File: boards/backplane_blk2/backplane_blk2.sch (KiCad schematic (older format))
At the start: 1 part, among them J1 Conn_04x24

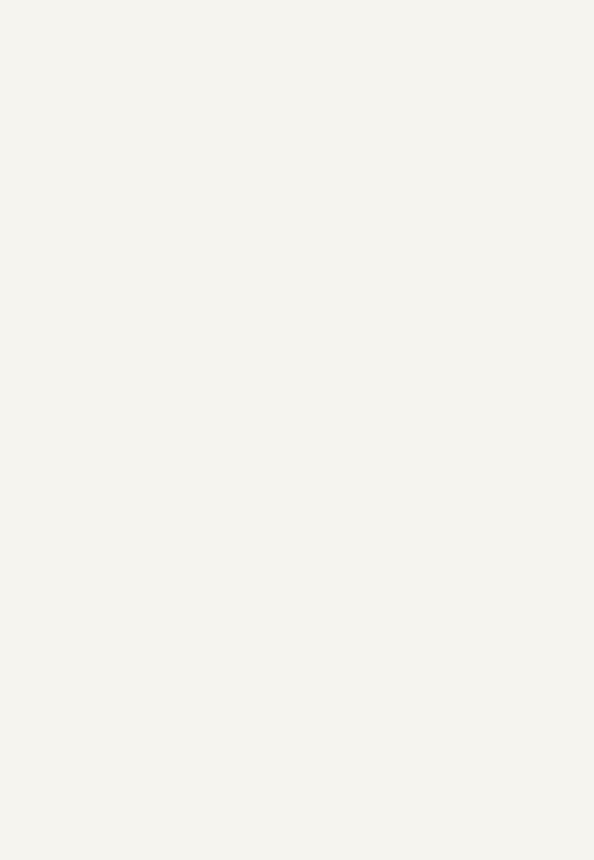
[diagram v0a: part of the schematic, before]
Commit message: Backplane board: new name, and initial integration of DIN-41612 3x32 C connector
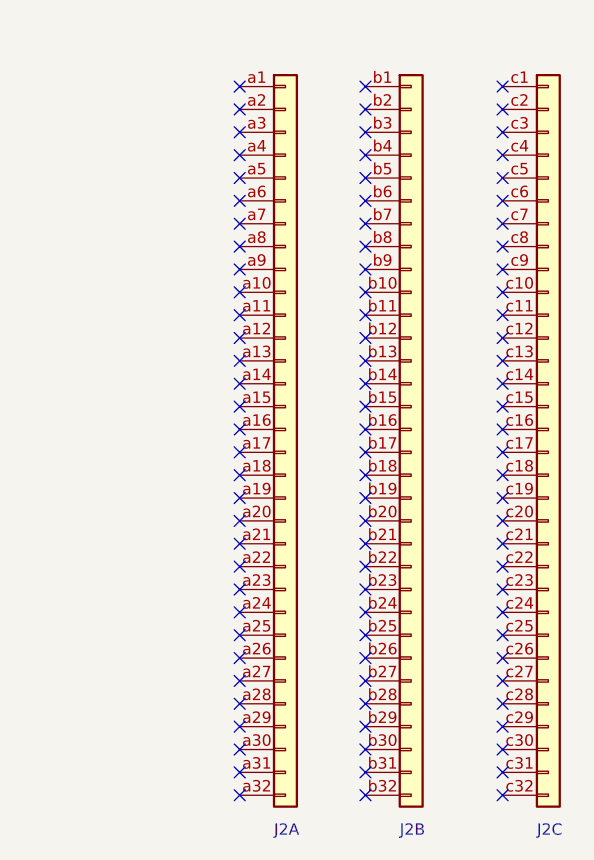
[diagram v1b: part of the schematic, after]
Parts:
- added J2: DIN41612_03x32_C, Connector_DIN:DIN41612_C_3x32_Female_Vertical_THT, symbol lachesis:DIN41612_03x32_C
- J1: footprint (none) -> lachesis:Rope_Connector
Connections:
- no-connect marks 6 -> 102
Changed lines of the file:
@@
 F 0 "J1" H 2400 700 50  0000 L CNN
 F 1 "Conn_04x24" H 2580 1951 50  0001 L CNN
-F 2 "" H 2500 2050 50  0001 C CNN
+F 2 "lachesis:Rope_Connector" H 2500 2050 50  0001 C CNN
 F 3 "~" H 2500 2050 50  0001 C CNN
 	1    2500 2050
@@
 F 0 "J1" H 3200 700 50  0000 L CNN
 F 1 "Conn_04x24" H 3380 1951 50  0001 L CNN
-F 2 "" H 3300 2050 50  0001 C CNN
+F 2 "lachesis:Rope_Connector" H 3300 2050 50  0001 C CNN
 F 3 "~" H 3300 2050 50  0001 C CNN
 	2    3300 2050
@@
 F 0 "J1" H 4000 700 50  0000 L CNN
 F 1 "Conn_04x24" H 4180 1951 50  0001 L CNN
-F 2 "" H 4100 2050 50  0001 C CNN
+F 2 "lachesis:Rope_Connector" H 4100 2050 50  0001 C CNN
 F 3 "~" H 4100 2050 50  0001 C CNN
 	3    4100 2050
@@
 NoConn ~ 3900 3250
 $Comp
-L power:GND #PWR?
+L power:GND #PWR0101
 U 1 1 617E1C61
 P 3500 750
-F 0 "#PWR?" H 3500 500 50  0001 C CNN
+F 0 "#PWR0101" H 3500 500 50  0001 C CNN
 F 1 "GND" H 3505 577 50  0000 C CNN
 F 2 "" H 3500 750 50  0001 C CNN
@@
 F 0 "J1" H 4800 700 50  0000 L CNN
 F 1 "Conn_04x24" H 4980 1951 50  0001 L CNN
-F 2 "" H 4900 2050 50  0001 C CNN
+F 2 "lachesis:Rope_Connector" H 4900 2050 50  0001 C CNN
 F 3 "~" H 4900 2050 50  0001 C CNN
 	4    4900 2050
@@
 Wire Wire Line
 	4700 3250 4650 3250
+$Comp
+L lachesis:DIN41612_03x32_C J2
+U 1 1 6198976A
+P 6950 2100
+F 0 "J2" H 6900 -50 50  0000 L CNN
+F 1 "DIN41612_03x32_C" H 6600 -150 50  0001 L CNN
+F 2 "Connector_DIN:DIN41612_C_3x32_Female_Vertical_THT" H 6950 2100 50  0001 C CNN
+F 3 "~" H 6950 2100 50  0001 C CNN
+	1    6950 2100
+	1    0    0    -1
+$EndComp
+$Comp
+L lachesis:DIN41612_03x32_C J2
+U 2 1 6198C67D
+P 7500 2100
+F 0 "J2" H 7450 -50 50  0000 L CNN
+F 1 "DIN41612_03x32_C" H 7150 -150 50  0001 L CNN
+F 2 "Connector_DIN:DIN41612_C_3x32_Female_Vertical_THT" H 7500 2100 50  0001 C CNN
+F 3 "~" H 7500 2100 50  0001 C CNN
+	2    7500 2100
+	1    0    0    -1
+$EndComp
+$Comp
+L lachesis:DIN41612_03x32_C J2
+U 3 1 61992140
+P 8100 2100
+F 0 "J2" H 8050 -50 50  0000 L CNN
+F 1 "DIN41612_03x32_C" H 7750 -150 50  0001 L CNN
+F 2 "Connector_DIN:DIN41612_C_3x32_Female_Vertical_THT" H 8100 2100 50  0001 C CNN
+F 3 "~" H 8100 2100 50  0001 C CNN
+	3    8100 2100
+	1    0    0    -1
+$EndComp
+NoConn ~ 6750 1000
+NoConn ~ 6750 1100
+NoConn ~ 6750 1200
+NoConn ~ 6750 1300
+NoConn ~ 6750 1400
+NoConn ~ 6750 1500
+NoConn ~ 6750 1600
+NoConn ~ 6750 1700
+NoConn ~ 6750 1800
+NoConn ~ 6750 1900
+NoConn ~ 6750 2000
+NoConn ~ 6750 2100
+NoConn ~ 6750 2200
+NoConn ~ 6750 2300
+NoConn ~ 6750 2400
+NoConn ~ 6750 2500
+NoConn ~ 6750 2600
+NoConn ~ 6750 2700
+NoConn ~ 6750 2800
+NoConn ~ 6750 2900
+NoConn ~ 6750 3000
+NoConn ~ 6750 3100
+NoConn ~ 6750 3200
+NoConn ~ 6750 3300
+NoConn ~ 6750 3400
+NoConn ~ 6750 3500
+NoConn ~ 6750 3600
+NoConn ~ 6750 3700
+NoConn ~ 6750 3800
+NoConn ~ 6750 3900
+NoConn ~ 6750 4000
+NoConn ~ 6750 4100
+NoConn ~ 7900 1000
+NoConn ~ 7900 1100
+NoConn ~ 7900 1200
+NoConn ~ 7900 1300
+NoConn ~ 7900 1400
+NoConn ~ 7900 1500
+NoConn ~ 7900 1600
+NoConn ~ 7900 1700
+NoConn ~ 7900 1800
+NoConn ~ 7900 1900
+NoConn ~ 7900 2000
+NoConn ~ 7900 2100
+NoConn ~ 7900 2200
+NoConn ~ 7900 2300
+NoConn ~ 7900 2400
+NoConn ~ 7900 2500
+NoConn ~ 7900 2600
+NoConn ~ 7900 2700
+NoConn ~ 7900 2800
+NoConn ~ 7900 2900
+NoConn ~ 7900 3000
+NoConn ~ 7900 3100
+NoConn ~ 7900 3200
+NoConn ~ 7900 3300
+NoConn ~ 7900 3400
+NoConn ~ 7900 3500
+NoConn ~ 7900 3600
+NoConn ~ 7900 3700
+NoConn ~ 7900 3800
+NoConn ~ 7900 3900
+NoConn ~ 7900 4000
+NoConn ~ 7900 4100
+NoConn ~ 7300 1000
+NoConn ~ 7300 1100
+NoConn ~ 7300 1200
+NoConn ~ 7300 1300
+NoConn ~ 7300 1400
+NoConn ~ 7300 1500
+NoConn ~ 7300 1600
+NoConn ~ 7300 1700
+NoConn ~ 7300 1800
+NoConn ~ 7300 1900
+NoConn ~ 7300 2000
+NoConn ~ 7300 2100
+NoConn ~ 7300 2200
+NoConn ~ 7300 2300
+NoConn ~ 7300 2400
+NoConn ~ 7300 2500
+NoConn ~ 7300 2600
+NoConn ~ 7300 2700
+NoConn ~ 7300 2800
+NoConn ~ 7300 2900
+NoConn ~ 7300 3000
+NoConn ~ 7300 3100
+NoConn ~ 7300 3200
+NoConn ~ 7300 3300
+NoConn ~ 7300 3400
+NoConn ~ 7300 3500
+NoConn ~ 7300 3600
+NoConn ~ 7300 3700
+NoConn ~ 7300 3800
+NoConn ~ 7300 3900
+NoConn ~ 7300 4000
+NoConn ~ 7300 4100
 $EndSCHEMATC
